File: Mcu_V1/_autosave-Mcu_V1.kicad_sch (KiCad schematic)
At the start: 22 parts, among them U1 24LC1025, U2 24LC1025, U3 ATMEGA328P-AU, Y1 Crystal, Y2 Crystal

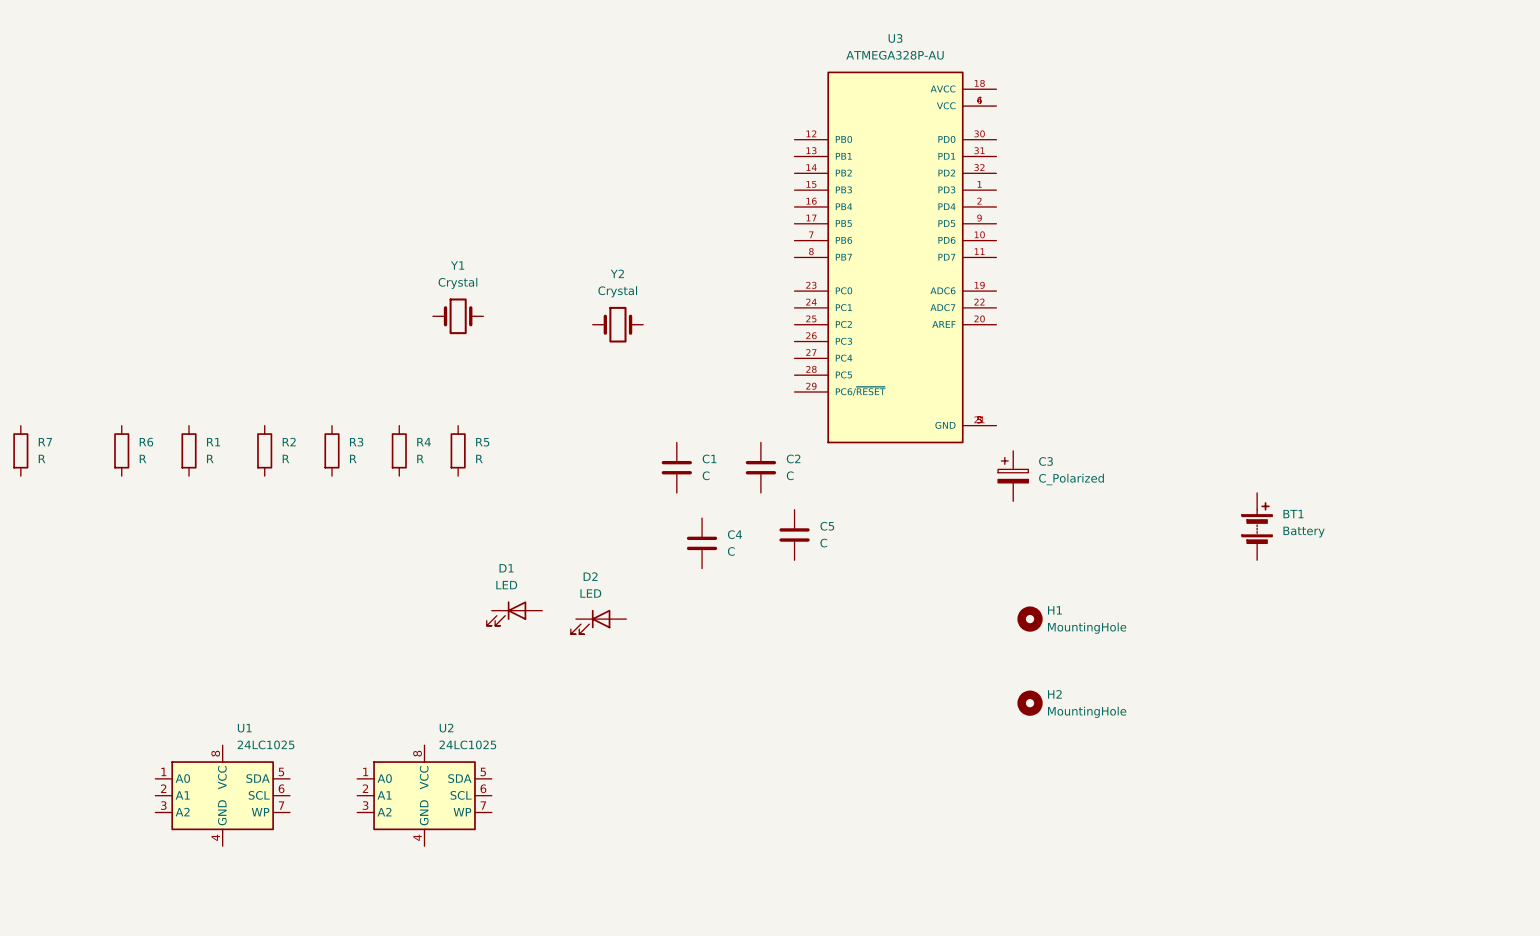
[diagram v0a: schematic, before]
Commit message: annotation Symbols
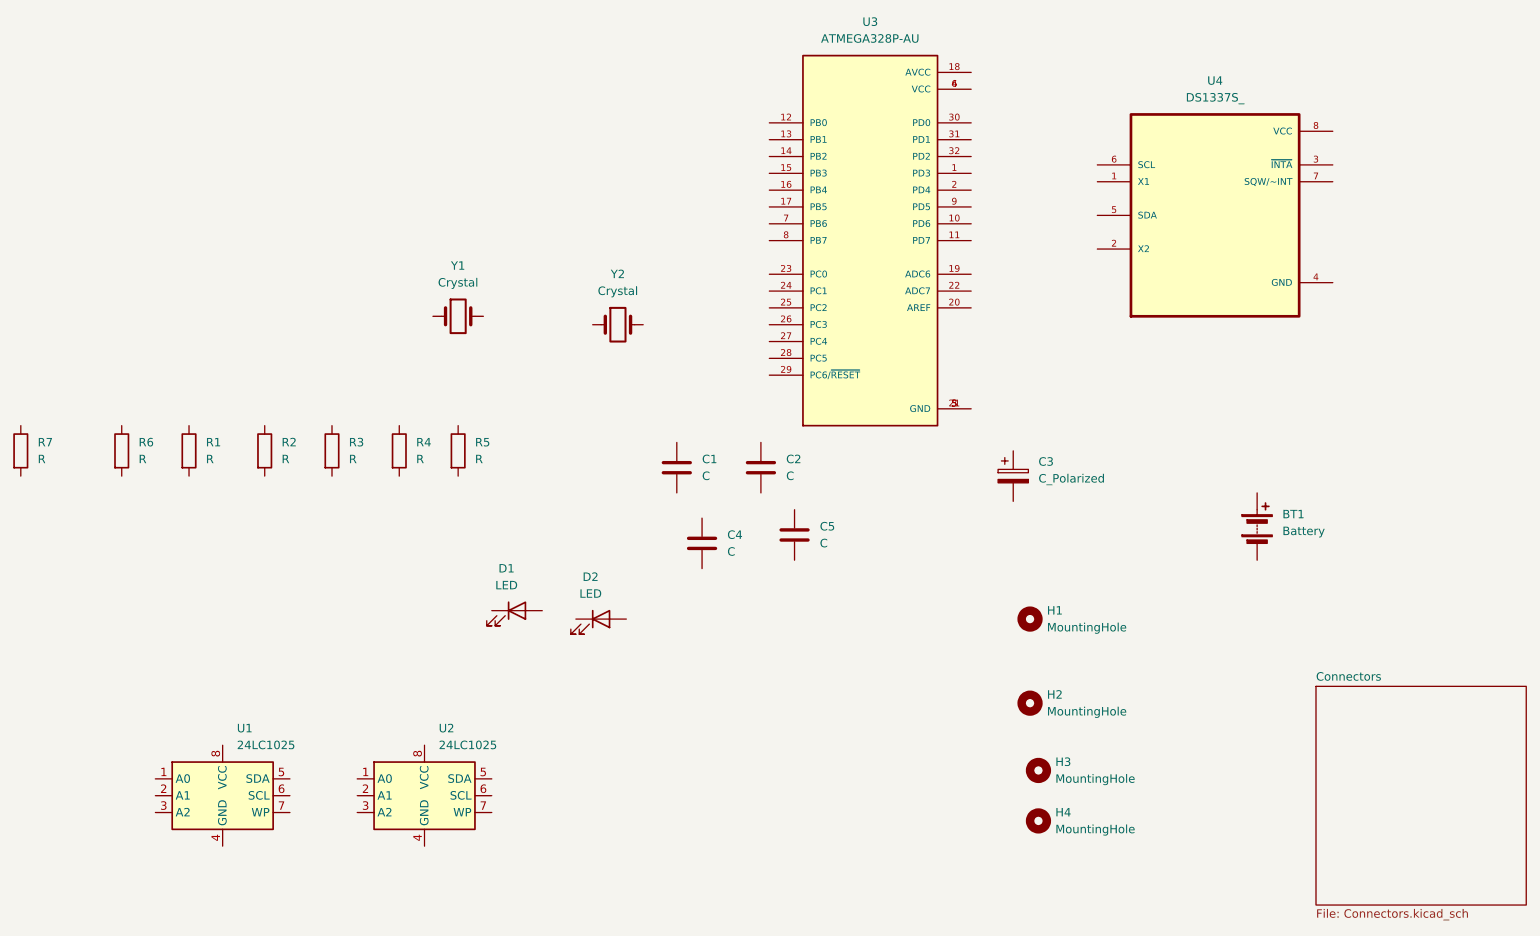
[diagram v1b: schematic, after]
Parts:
- added H3, H4: MountingHole, symbol Mechanical:MountingHole
- added U4: DS1337S_, DS1337S_:SOIC127P600X175-8N, symbol DS1337S_:DS1337S_
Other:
- added sheet Connectors (Connectors.kicad_sch)
- moved on the sheet: U3
